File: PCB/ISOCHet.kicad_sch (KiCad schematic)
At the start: 19 parts, among them J1 USB_C_Receptacle_USB2.0, J2 Conn_01x08_Pin, SW0 BOOT, SW1 TAB, SW2 ENTER, SW3 CAPS, SW4 CAPS_STEP1.5, SW5 CAPS_STEP1.25, U1 CH552G, U2 USBLC6-2P6

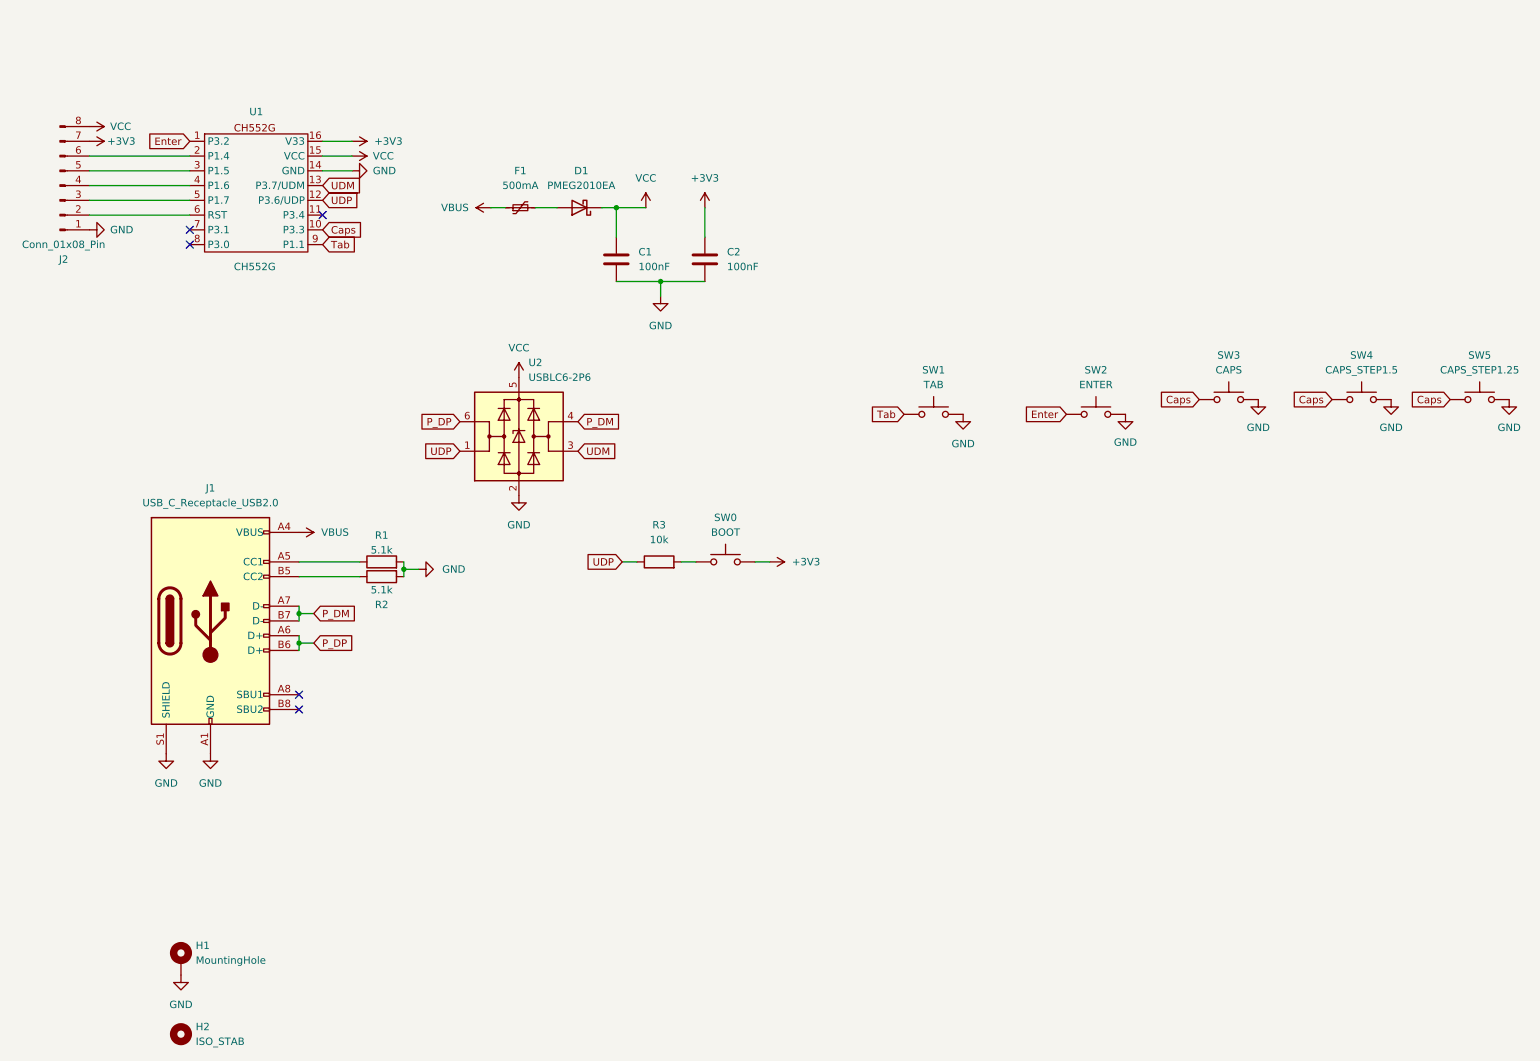
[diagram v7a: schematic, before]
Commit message: Tidy up schematic
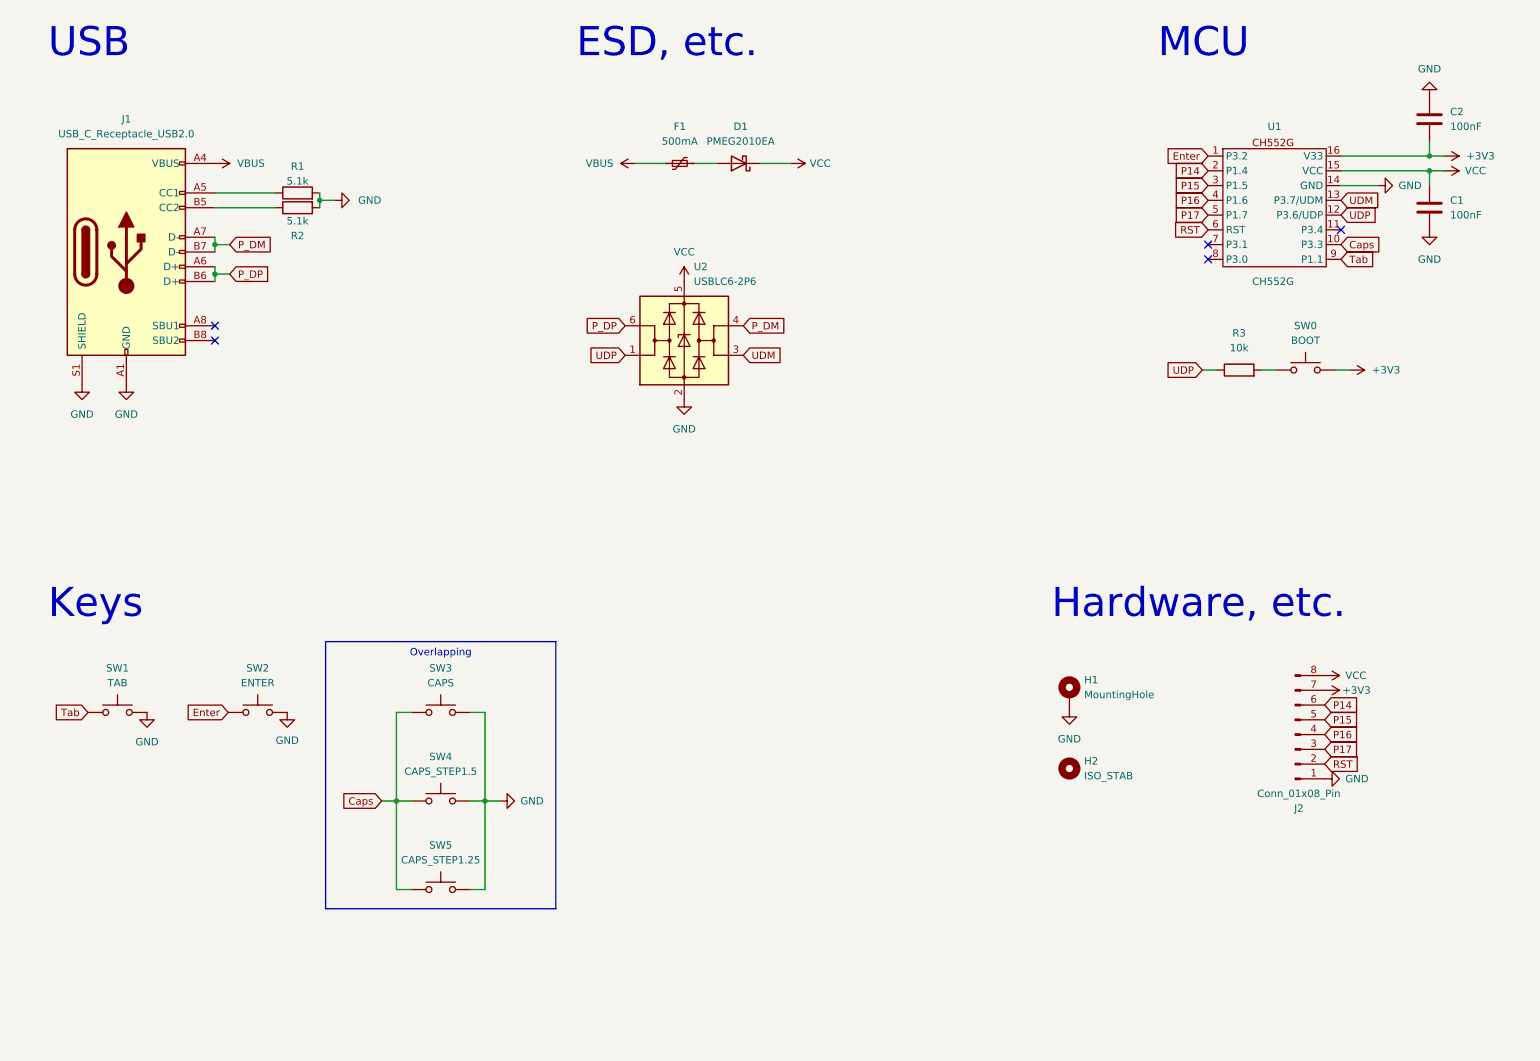
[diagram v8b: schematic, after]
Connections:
- net RST: now reaches J2.2 (Pin_2), U1.6 (RST)
- net P17: now reaches J2.3 (Pin_3), U1.5 (P1.7)
- net P16: now reaches J2.4 (Pin_4), U1.4 (P1.6)
- net P15: now reaches J2.5 (Pin_5), U1.3 (P1.5)
- net P14: now reaches J2.6 (Pin_6), U1.2 (P1.4)
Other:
- note added: "ESD, etc."
- note added: "Hardware, etc."
- note added: "Keys"
- note added: "MCU"
- note added: "USB"
- company: (none) -> u/bgkendall
- title: (none) -> ISOCHet
- moved on the sheet: D1, F1, H1, H2, J1, J2, R1, R2, R3, SW0, SW1, SW2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
